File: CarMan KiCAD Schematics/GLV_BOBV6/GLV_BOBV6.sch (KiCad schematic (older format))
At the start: 8 parts, among them J1 2PinPortRight, J2 2PinPortRight, J3 4PinPort, J4 4PinPort, J5 2PinPortRight, J6 2PinPortLeft, J7 2PinPortRight

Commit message: GLV Schematic/Library Update
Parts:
- removed J3: 4PinPort, symbol CarMan_KiCAD_Library:4PinPort
- removed J6: 2PinPortLeft, symbol CarMan_KiCAD_Library:2PinPortLeft
- removed U?: 2PinPortRight, symbol CarMan_KiCAD_Library:2PinPortRight
- added C? (x2): 0.1uF, symbol Device:C
- added C?: 1uF, symbol Device:C
- added C?: 0.47uF, symbol Device:C
- added C?: 0.33uF, symbol Device:C
- added CR?: L78L05ACD13TR, SO-8_STM, symbol CarMan_KiCAD_Library:L78L05ACD13TR
- added R?: 10K, symbol Device:R
- added U?: DCR012405U, DVB12, symbol CarMan_KiCAD_Library:DCR012405U
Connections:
- net 5V_ISO: now also C?.2, R?.2, U?.14 (VO)
- net 5V_NOT_ISO: now also C?.1, CR?.8 (VIN)
- net GLV_I2C_RTN: now also C?.1, C?.2, U?.13 (OVOUT)
- net GLV_RTN: now also J2.2, J5.2, J7.2, C?.1, C?.2, C?.2, CR?.2 (GND), CR?.3 (GND), CR?.6 (GND), CR?.7 (GND), U?.27 (OVIN)
- net 24V_ISO renamed 24V
- net 24V: now also J7.1, C?.1, C?.2, CR?.1 (VOUT), U?.1 (VS); no longer J7.2
- removed net ISO_RTN: J2.2, J5.2, J7.1
- new net: C?.1, U?.12 (VREC), U?.16 (ENABLE)
- new net: R?.1, U?.17 (*ERROR)
- no-connect marks 2 -> 5

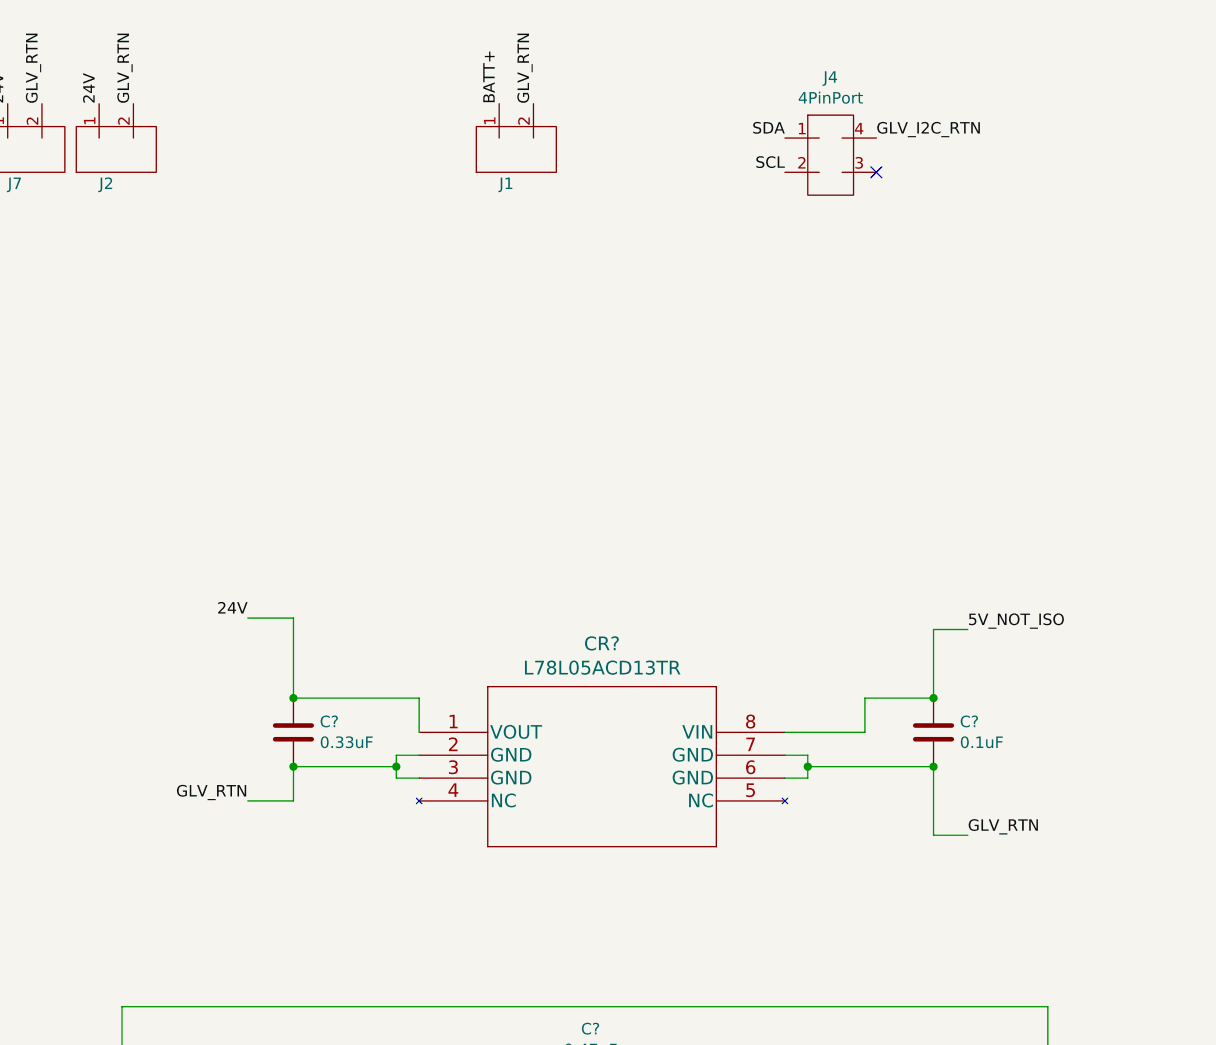
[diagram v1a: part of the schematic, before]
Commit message: GLV Schematic Fix - Logic Power
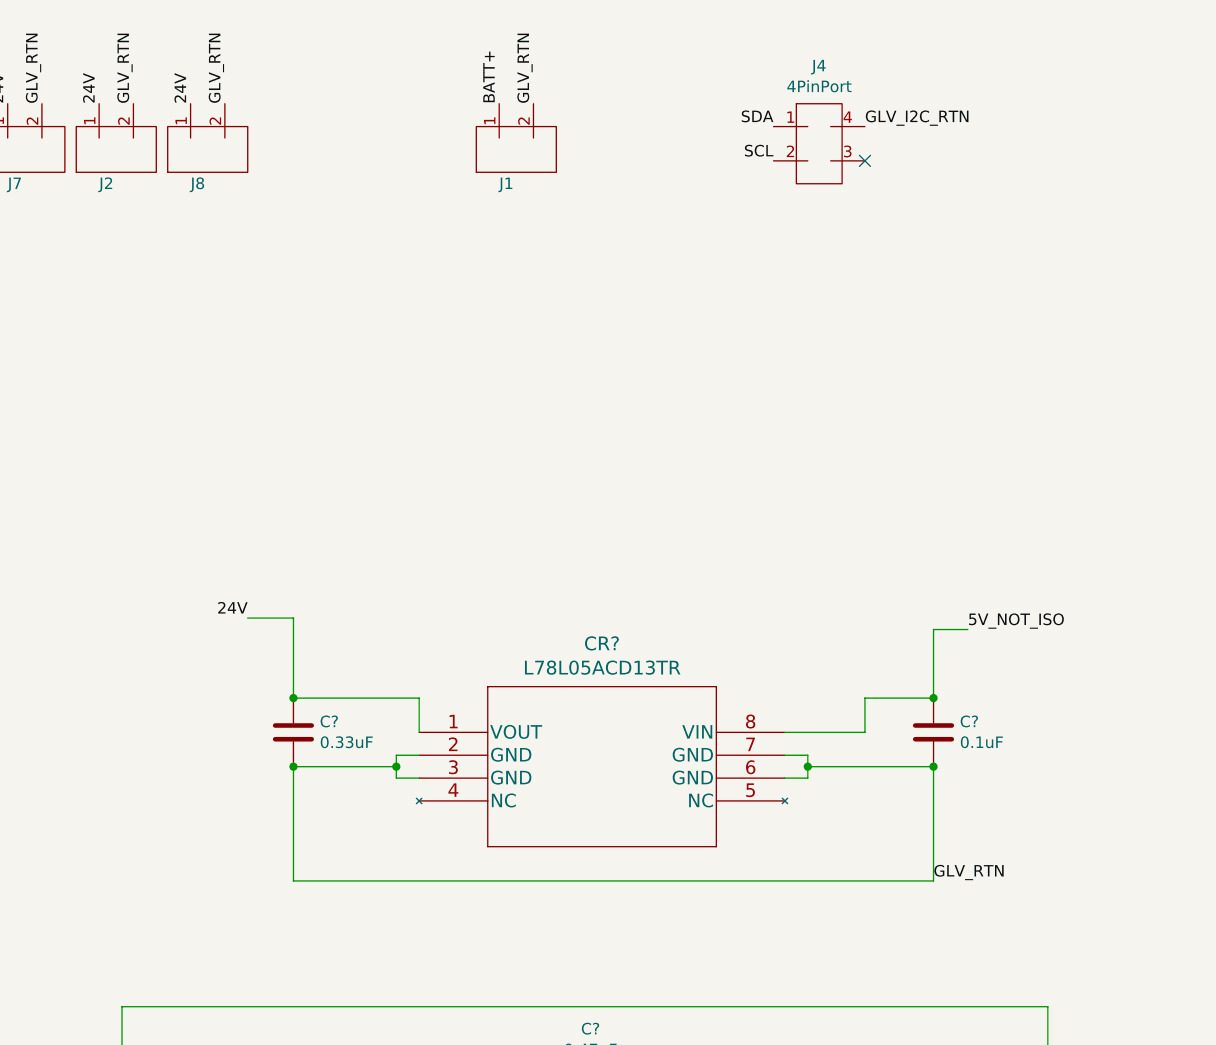
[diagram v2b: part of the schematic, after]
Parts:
- added J8: 2PinPortRight, symbol CarMan_KiCAD_Library:2PinPortRight
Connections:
- net 24V: now also J8.1
- net GLV_RTN: now also J8.2
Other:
- moved on the sheet: J4
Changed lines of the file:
@@
 Text Label 1900 1000 1    50   ~ 0
 GLV_RTN
-Text Label 4750 1150 2    50   ~ 0
+Text Label 4700 1100 2    50   ~ 0
 SDA
-Text Label 4750 1300 2    50   ~ 0
+Text Label 4700 1250 2    50   ~ 0
 SCL
-Text Label 5150 1150 0    50   ~ 0
+Text Label 5100 1100 0    50   ~ 0
 GLV_I2C_RTN
-NoConn ~ 5150 1300
+NoConn ~ 5100 1250
 Text Label 1350 1000 1    50   ~ 0
 24V
@@
 L CarMan_KiCAD_Library:4PinPort J4
 U 1 1 5F96011A
-P 4950 1200
-F 0 "J4" H 4950 1515 50  0000 C CNN
-F 1 "4PinPort" H 4950 1424 50  0000 C CNN
-F 2 "" H 4850 1300 50  0001 C CNN
-F 3 "" H 4850 1300 50  0001 C CNN
-	1    4950 1200
+P 4900 1150
+F 0 "J4" H 4900 1465 50  0000 C CNN
+F 1 "4PinPort" H 4900 1374 50  0000 C CNN
+F 2 "" H 4800 1250 50  0001 C CNN
+F 3 "" H 4800 1250 50  0001 C CNN
+	1    4900 1150
 	1    0    0    -1
 $EndComp
@@
 Text Label 5550 3300 0    50   ~ 0
 5V_NOT_ISO
-Wire Wire Line
-	5400 3900 5400 4200
-Wire Wire Line
-	5400 4200 5550 4200
 Connection ~ 5400 3900
-Text Label 5550 4200 0    50   ~ 0
+Text Label 5400 4400 0    50   ~ 0
 GLV_RTN
 Wire Wire Line
@@
 	2600 3250 2400 3250
 Connection ~ 2600 3600
-Wire Wire Line
-	2600 3900 2600 4050
 Connection ~ 2600 3900
-Wire Wire Line
-	2600 4050 2400 4050
 Text Label 2400 3250 2    50   ~ 0
 24V
-Text Label 2400 4050 2    50   ~ 0
-GLV_RTN
+Text Label 2150 1000 1    50   ~ 0
+24V
+Text Label 2300 1000 1    50   ~ 0
+GLV_RTN
+$Comp
+L CarMan_KiCAD_Library:2PinPortRight J8
+U 1 1 5F97AF06
+P 2200 1200
+F 0 "J8" V 2050 1250 50  0000 R CNN
+F 1 "2PinPortRight" V 2213 972 50  0001 R CNN
+F 2 "" H 2200 1200 50  0001 C CNN
+F 3 "" H 2200 1200 50  0001 C CNN
+	1    2200 1200
+	0    -1   -1   0
+$EndComp
+Wire Wire Line
+	2600 4400 5400 4400
+Wire Wire Line
+	2600 3900 2600 4400
+Wire Wire Line
+	5400 3900 5400 4400
 $EndSCHEMATC

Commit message: GLV Comment
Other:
- note added: "GLV_I2C_RTN = 5V_ISO_RTN"
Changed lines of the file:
@@
 Wire Wire Line
 	5400 3900 5400 4400
+Text Notes 8250 3100 0    50   ~ 0
+GLV_I2C_RTN = 5V_ISO_RTN
 $EndSCHEMATC

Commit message: GLV Tentatively Finished
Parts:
- added 24V: PWR_FLAG, symbol power:PWR_FLAG
- added D1, D? (x2): LED, symbol Device:LED
- added H1: MountingHole_Pad, symbol Mechanical:MountingHole_Pad
- added R7, R8: 200, symbol Device:R
- added R9: 5K, symbol Device:R
- added U?: J15, symbol CarMan_KiCAD_Library:2PinPortLeft
- gave numbers to parts that had none: 6
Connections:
- net 24V: now also U1.2 (VS), 24V.1 (pwr), R9.2, U?.2
- net 5V_ISO: now also R7.2
- net 5V_NOT_ISO: now also R8.2
- net GLV_I2C_RTN: now also D1.1 (K)
- net GLV_RTN: now also U1.26 (OVIN), D?.1 (K), D?.1 (K), U?.1
- new net: D1.2 (A), R7.1
- new net: D?.2 (A), R8.1
- new net: D?.2 (A), R9.1
- new net CHASS_GND: H1.1
- no-connect marks 5 -> 3
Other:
- note added: "24V to Battery Packs"
- note added: "24V to Can ISO for Motor Controller"
- note added: "24V to Dash/EPAL"
- note added: "24V to TSI/Analog Board"
- note added: "Connection to Logic Board for the I2C line. Runs on Carman's internal W9 wire."
- note added: "Current/Voltage Sensor and I2C Isolator"
- note added: "Extra 24V\n"
- note added: "From LSP"
- note added: "Isolated DC/DC 24V to 5V"
- note added: "Non-Isolated DC/DC 24V to 5V"
- note added: "Note: Caps for the isolator must be placed close to the pins and must be low ESR, ceramic capacitors."
- note added: "Status Lights"
- note added: "Voltage(s) and Ground(s) that other boards see"
- moved on the sheet: J1, J2, J4, J5, J7, J8

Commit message: GLV Tentatively Finished with part labels
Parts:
- gave numbers to parts that had none: 4
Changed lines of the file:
@@
 $EndComp
 $Comp
-L Device:C C?
+L Device:C C6
 U 1 1 5F9993A2
 P 5400 3750
-F 0 "C?" H 5515 3796 50  0000 L CNN
+F 0 "C6" H 5515 3796 50  0000 L CNN
 F 1 "0.1uF" H 5515 3705 50  0000 L CNN
 F 2 "" H 5438 3600 50  0001 C CNN
@@
 	3050 3950 3150 3950
 $Comp
-L Device:C C?
+L Device:C C5
 U 1 1 5F9A004E
 P 2600 3750
-F 0 "C?" H 2715 3796 50  0000 L CNN
+F 0 "C5" H 2715 3796 50  0000 L CNN
 F 1 "0.33uF" H 2715 3705 50  0000 L CNN
 F 2 "" H 2638 3600 50  0001 C CNN
@@
 $EndComp
 $Comp
-L Device:LED D?
+L Device:LED D2
 U 1 1 5F9B456F
 P 10100 2200
-F 0 "D?" V 10139 2082 50  0000 R CNN
+F 0 "D2" V 10139 2082 50  0000 R CNN
 F 1 "LED" V 10048 2082 50  0000 R CNN
 F 2 "" H 10100 2200 50  0001 C CNN
@@
 $EndComp
 $Comp
-L Device:LED D?
+L Device:LED D3
 U 1 1 5F9B4BC9
 P 10600 2200
-F 0 "D?" V 10639 2082 50  0000 R CNN
+F 0 "D3" V 10639 2082 50  0000 R CNN
 F 1 "LED" V 10548 2082 50  0000 R CNN
 F 2 "" H 10600 2200 50  0001 C CNN

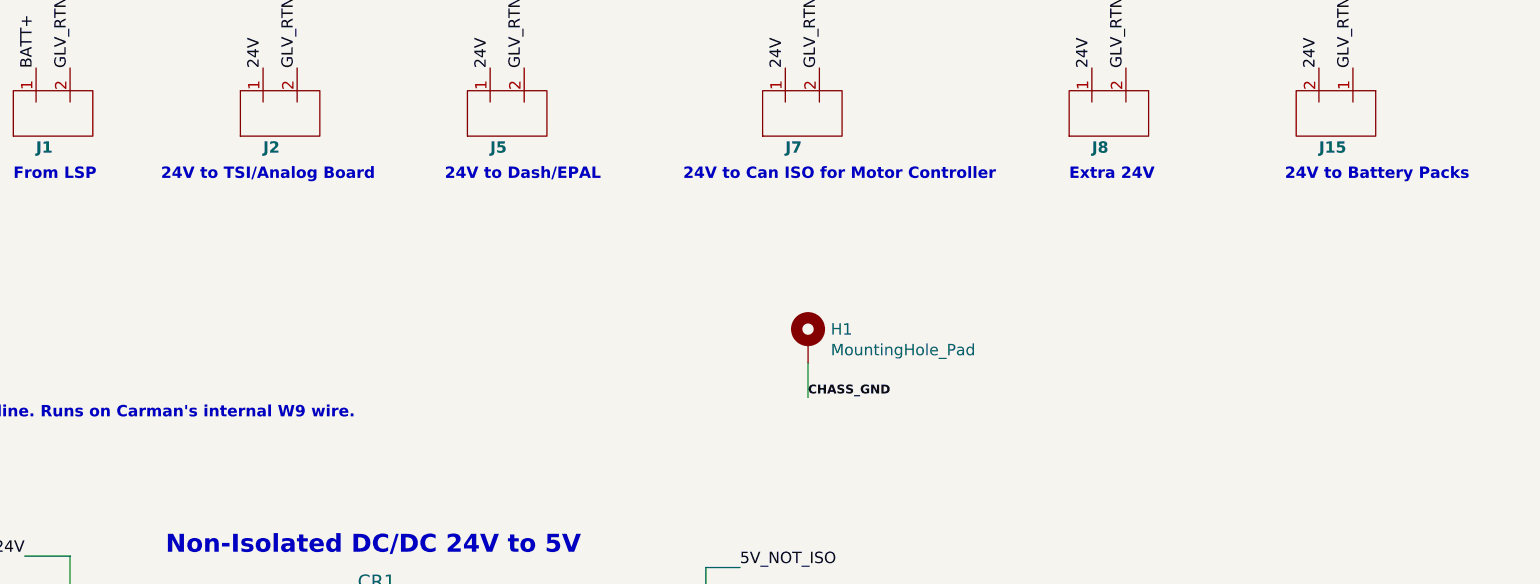
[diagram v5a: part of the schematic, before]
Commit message: GLV with Cooling Connector
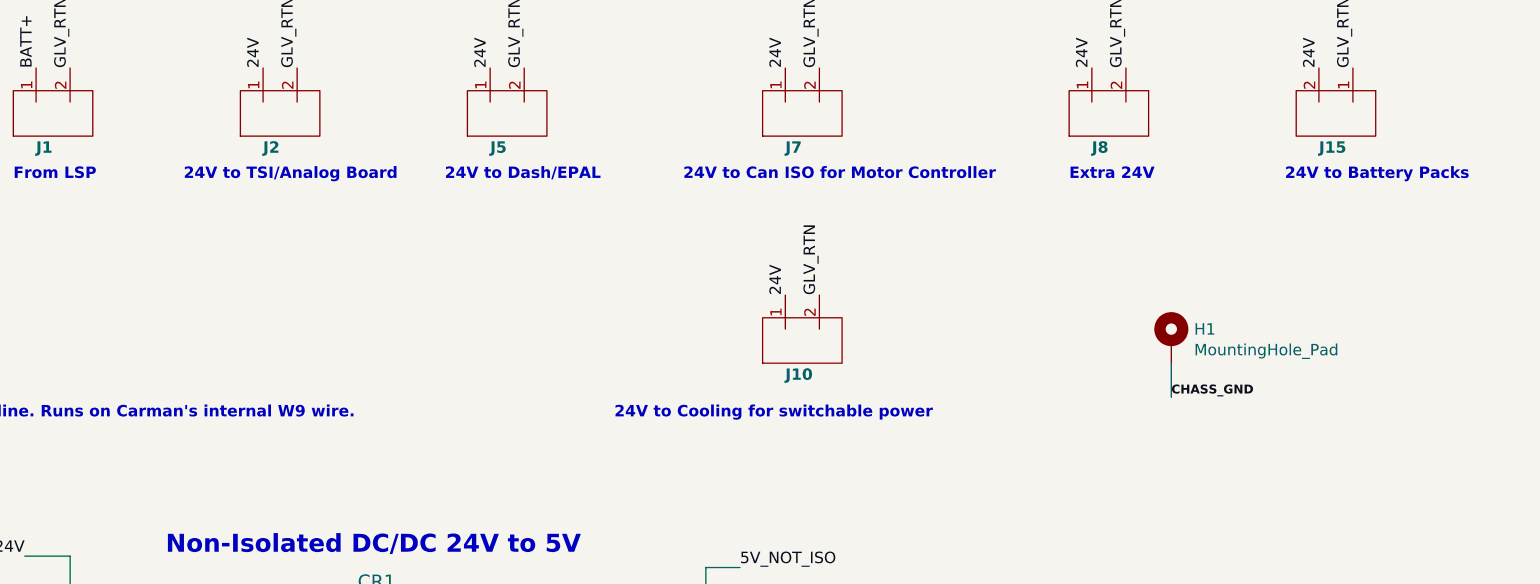
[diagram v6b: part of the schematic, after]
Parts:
- added J10: 2PinPortRight, symbol CarMan_KiCAD_Library:2PinPortRight
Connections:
- net 24V: now also J10.1
- net GLV_RTN: now also J10.2
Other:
- note added: "24V to Cooling for switchable power"
- moved on the sheet: H1
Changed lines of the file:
@@
 Text Notes 2350 1600 0    50   ~ 10
 From LSP
-Text Notes 3000 1600 0    50   ~ 10
+Text Notes 3100 1600 0    50   ~ 10
 24V to TSI/Analog Board
 Text Notes 4250 1600 0    50   ~ 10
@@
 L Mechanical:MountingHole_Pad H1
 U 1 1 5F9DCEB0
-P 5850 2300
-F 0 "H1" H 5950 2349 50  0000 L CNN
-F 1 "MountingHole_Pad" H 5950 2258 50  0000 L CNN
-F 2 "" H 5850 2300 50  0001 C CNN
-F 3 "~" H 5850 2300 50  0001 C CNN
-	1    5850 2300
-	1    0    0    -1
-$EndComp
-Wire Wire Line
-	5850 2400 5850 2550
-Text Label 5850 2550 0    39   ~ 8
+P 7450 2300
+F 0 "H1" H 7550 2349 50  0000 L CNN
+F 1 "MountingHole_Pad" H 7550 2258 50  0000 L CNN
+F 2 "" H 7450 2300 50  0001 C CNN
+F 3 "~" H 7450 2300 50  0001 C CNN
+	1    7450 2300
+	1    0    0    -1
+$EndComp
+Wire Wire Line
+	7450 2400 7450 2550
+Text Label 7450 2550 0    39   ~ 8
 CHASS_GND
+Text Label 5750 2100 1    50   ~ 0
+24V
+Text Label 5900 2100 1    50   ~ 0
+GLV_RTN
+$Comp
+L CarMan_KiCAD_Library:2PinPortRight J10
+U 1 1 5F98EB64
+P 5800 2300
+F 0 "J10" V 5650 2350 50  0000 R CNB
+F 1 "2PinPortRight" V 5813 2072 50  0001 R CNN
+F 2 "" H 5800 2300 50  0001 C CNN
+F 3 "" H 5800 2300 50  0001 C CNN
+	1    5800 2300
+	0    -1   -1   0
+$EndComp
+Text Notes 6400 2650 2    50   ~ 10
+24V to Cooling for switchable power
 $EndSCHEMATC
